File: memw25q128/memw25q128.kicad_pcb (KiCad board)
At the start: 2 copper layers, 76.2 x 50.8 mm, 15 parts, among them J1 STM32WORLD_BASE, U1 W25Q128JVS

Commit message: Hmmm
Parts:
- U1: footprint Package_SO:SOIC-8_5.23x5.23mm_P1.27mm -> Package_SO:SOIC-8_5.275x5.275mm_P1.27mm
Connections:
- J1 pad 10: Net-(J1-Pad10) -> unconnected-(J1-Pad10)
- J1 pad 11: Net-(J1-Pad11) -> unconnected-(J1-Pad11)
- J1 pad 12: Net-(J1-Pad12) -> unconnected-(J1-Pad12)
- J1 pad 17: Net-(J1-Pad17) -> unconnected-(J1-Pad17)
- J1 pad 18: Net-(J1-Pad18) -> unconnected-(J1-Pad18)
- J1 pad 19: Net-(J1-Pad19) -> unconnected-(J1-Pad19)
- J1 pad 20: Net-(J1-Pad20) -> unconnected-(J1-Pad20)
- J1 pad 21: Net-(J1-Pad21) -> unconnected-(J1-Pad21)
- J1 pad 22: Net-(J1-Pad22) -> unconnected-(J1-Pad22)
- J1 pad 23: Net-(J1-Pad23) -> unconnected-(J1-Pad23)
- J1 pad 24: Net-(J1-Pad24) -> unconnected-(J1-Pad24)
- J1 pad 29: Net-(J1-Pad29) -> unconnected-(J1-Pad29)
- J1 pad 3: Net-(J1-Pad3) -> unconnected-(J1-Pad3)
- J1 pad 30: Net-(J1-Pad30) -> unconnected-(J1-Pad30)
- J1 pad 31: Net-(J1-Pad31) -> unconnected-(J1-Pad31)
- J1 pad 32: Net-(J1-Pad32) -> unconnected-(J1-Pad32)
- J1 pad 33: Net-(J1-Pad33) -> unconnected-(J1-Pad33)
- J1 pad 34: Net-(J1-Pad34) -> unconnected-(J1-Pad34)
- J1 pad 35: Net-(J1-Pad35) -> unconnected-(J1-Pad35)
- J1 pad 36: Net-(J1-Pad36) -> unconnected-(J1-Pad36)
- J1 pad 39: Net-(J1-Pad39) -> unconnected-(J1-Pad39)
- J1 pad 4: Net-(J1-Pad4) -> unconnected-(J1-Pad4)
- J1 pad 41: Net-(J1-Pad41) -> unconnected-(J1-Pad41)
- J1 pad 45: Net-(J1-Pad45) -> unconnected-(J1-Pad45)
- J1 pad 46: Net-(J1-Pad46) -> unconnected-(J1-Pad46)
- J1 pad 47: Net-(J1-Pad47) -> unconnected-(J1-Pad47)
- J1 pad 48: Net-(J1-Pad48) -> unconnected-(J1-Pad48)
- J1 pad 49: Net-(J1-Pad49) -> unconnected-(J1-Pad49)
- J1 pad 5: Net-(J1-Pad5) -> unconnected-(J1-Pad5)
- J1 pad 50: Net-(J1-Pad50) -> unconnected-(J1-Pad50)
- J1 pad 51: Net-(J1-Pad51) -> unconnected-(J1-Pad51)
- J1 pad 52: Net-(J1-Pad52) -> unconnected-(J1-Pad52)
- J1 pad 53: Net-(J1-Pad53) -> unconnected-(J1-Pad53)
- J1 pad 54: Net-(J1-Pad54) -> unconnected-(J1-Pad54)
- J1 pad 55: Net-(J1-Pad55) -> unconnected-(J1-Pad55)
- J1 pad 57: Net-(J1-Pad57) -> unconnected-(J1-Pad57)
- J1 pad 58: Net-(J1-Pad58) -> unconnected-(J1-Pad58)
- J1 pad 59: Net-(J1-Pad59) -> unconnected-(J1-Pad59)
- J1 pad 6: Net-(J1-Pad6) -> unconnected-(J1-Pad6)
- J1 pad 60: Net-(J1-Pad60) -> unconnected-(J1-Pad60)
- J1 pad 61: Net-(J1-Pad61) -> unconnected-(J1-Pad61)
- J1 pad 62: Net-(J1-Pad62) -> unconnected-(J1-Pad62)
- J1 pad 63: Net-(J1-Pad63) -> unconnected-(J1-Pad63)
- J1 pad 67: Net-(J1-Pad67) -> unconnected-(J1-Pad67)
- J1 pad 68: Net-(J1-Pad68) -> unconnected-(J1-Pad68)
- J1 pad 69: Net-(J1-Pad69) -> unconnected-(J1-Pad69)
- J1 pad 7: Net-(J1-Pad7) -> unconnected-(J1-Pad7)
- J1 pad 70: Net-(J1-Pad70) -> unconnected-(J1-Pad70)
- J1 pad 71: Net-(J1-Pad71) -> unconnected-(J1-Pad71)
- J1 pad 72: Net-(J1-Pad72) -> unconnected-(J1-Pad72)
- J1 pad 73: Net-(J1-Pad73) -> unconnected-(J1-Pad73)
- J1 pad 74: Net-(J1-Pad74) -> unconnected-(J1-Pad74)
- J1 pad 75: Net-(J1-Pad75) -> unconnected-(J1-Pad75)
- J1 pad 76: Net-(J1-Pad76) -> unconnected-(J1-Pad76)
- J1 pad 77: Net-(J1-Pad77) -> unconnected-(J1-Pad77)
- J1 pad 78: Net-(J1-Pad78) -> unconnected-(J1-Pad78)
- J1 pad 8: Net-(J1-Pad8) -> unconnected-(J1-Pad8)
- J1 pad 80: Net-(J1-Pad80) -> unconnected-(J1-Pad80)
- J1 pad 9: Net-(J1-Pad9) -> unconnected-(J1-Pad9)
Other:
- net class Default removed

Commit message: Hmmmm
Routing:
- net CLK: track 60.2 -> 62.7 mm
- net CS: track 61.5 -> 63.4 mm
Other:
- board text added: "${TITLE}"

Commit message: Playing with ordering files
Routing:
- net PA15: track 50.7 -> 51.6 mm
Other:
- board text removed: "${TITLE}"

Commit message: Still messing with ordering files
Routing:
- net CS: track 63.4 -> 65.8 mm
- net PB15: track 23.7 -> 24.8 mm
- net CLK: track 62.7 -> 63.2 mm

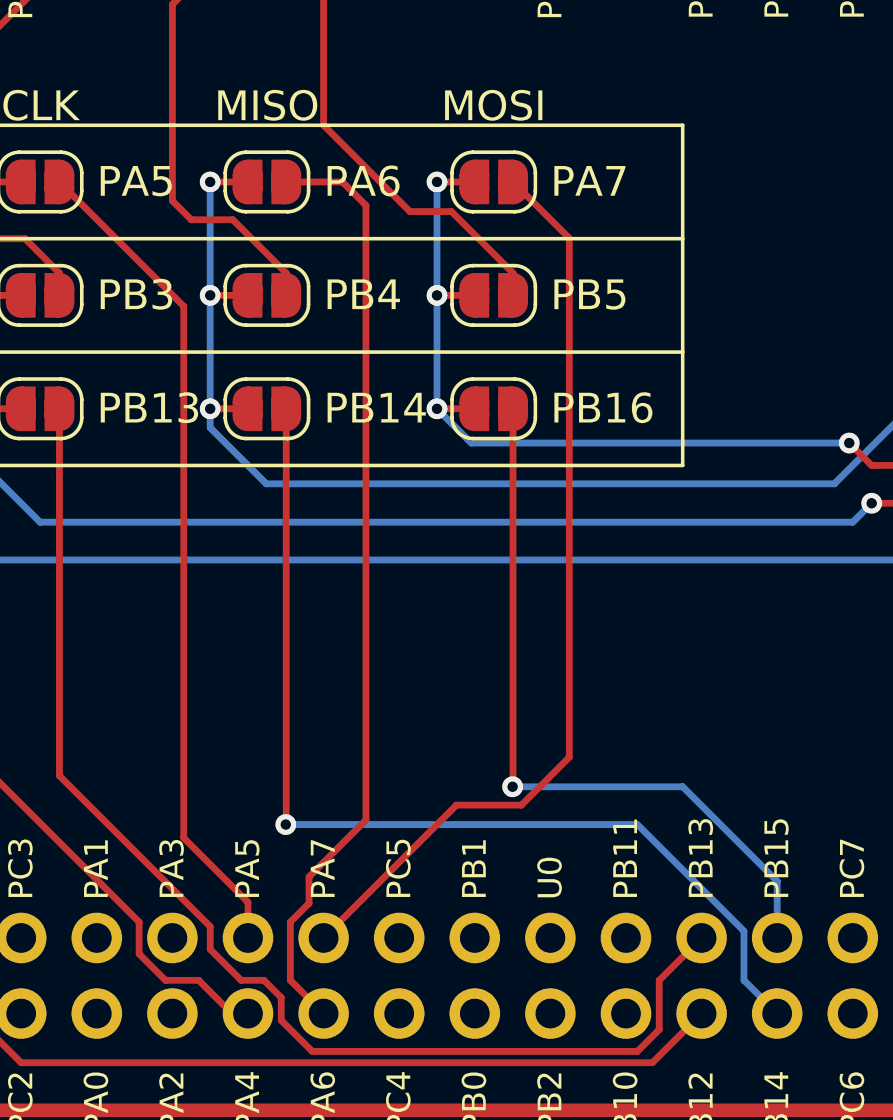
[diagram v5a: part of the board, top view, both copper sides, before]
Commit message: memw25q128 order files done and working
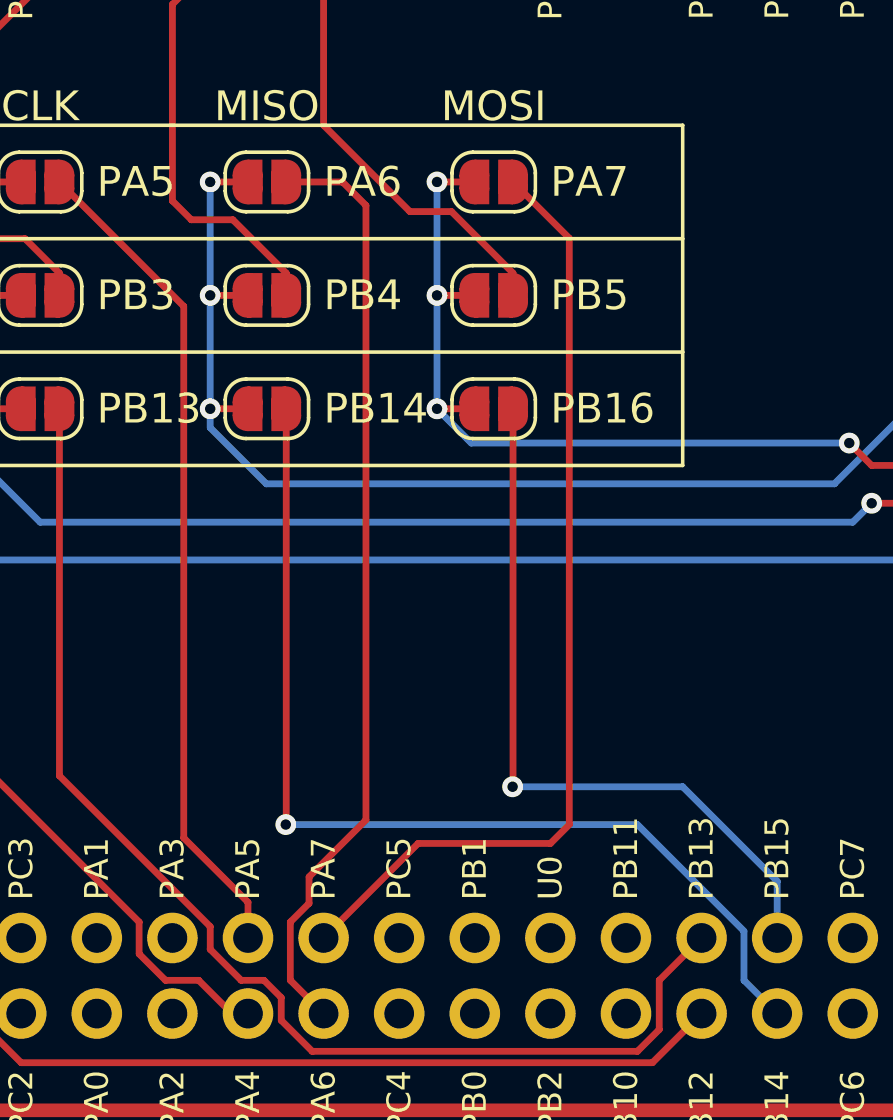
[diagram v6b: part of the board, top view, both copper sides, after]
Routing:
- net PA7: track 30.9 -> 32.2 mm
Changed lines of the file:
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@@
   (setup
     (pad_to_mask_clearance 0)
-    (aux_axis_origin 108.585 122.555)
-    (grid_origin 108.585 122.555)
+    (aux_axis_origin 106.68 124.46)
+    (grid_origin 106.68 124.46)
     (pcbplotparams
       (layerselection 0x00010fc_ffffffff)
@@
   (segment (start 140.97 89.535) (end 139.08 89.535) (width 0.2286) (layer "F.Cu") (net 64))
   (segment (start 141.758299 90.323299) (end 140.97 89.535) (width 0.2286) (layer "F.Cu") (net 64))
-  (segment (start 146.7 89.535) (end 148.59 91.425) (width 0.2286) (layer "F.Cu") (net 65))
-  (segment (start 144.798298 110.471702) (end 140.335 114.935) (width 0.2286) (layer "F.Cu") (net 65))
-  (segment (start 146.981018 110.471702) (end 144.798298 110.471702) (width 0.2286) (layer "F.Cu") (net 65))
-  (segment (start 148.59 91.425) (end 148.59 108.86272) (width 0.2286) (layer "F.Cu") (net 65))
-  (segment (start 148.59 108.86272) (end 146.981018 110.471702) (width 0.2286) (layer "F.Cu") (net 65))
+  (segment (start 148.59 111.125) (end 148.59 91.425) (width 0.2286) (layer "F.Cu") (net 65))
+  (segment (start 147.955 111.76) (end 148.59 111.125) (width 0.2286) (layer "F.Cu") (net 65))
+  (segment (start 143.51 111.76) (end 147.955 111.76) (width 0.2286) (layer "F.Cu") (net 65))
+  (segment (start 148.59 91.425) (end 146.7 89.535) (width 0.2286) (layer "F.Cu") (net 65))
+  (segment (start 140.335 114.935) (end 143.51 111.76) (width 0.2286) (layer "F.Cu") (net 65))
   (segment (start 127.405581 116.358299) (end 128.171017 116.358299) (width 0.2286) (layer "F.Cu") (net 66))
   (segment (start 126.518299 115.471017) (end 127.405581 116.358299) (width 0.2286) (layer "F.Cu") (net 66))

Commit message: memw25q128 order files confirmed
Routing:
- net GND: vias 0 -> 21

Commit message: Hmmmm
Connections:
- J1 pad 1: +3V3 -> unconnected-(J1-Pad1)
- J1 pad 79: +3V3 -> unconnected-(J1-Pad79)
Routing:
- net +3V3: track 145.0 -> 46.7 mm
